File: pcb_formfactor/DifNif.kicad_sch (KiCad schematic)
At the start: 27 parts, among them J2 PROG, J4 HPLA_PORT, U1 ICE40HX4K-TQ144, U13 Teensy4_1, U2 SST26VF080A-104I/SN, X1 ASE-xxxMHz

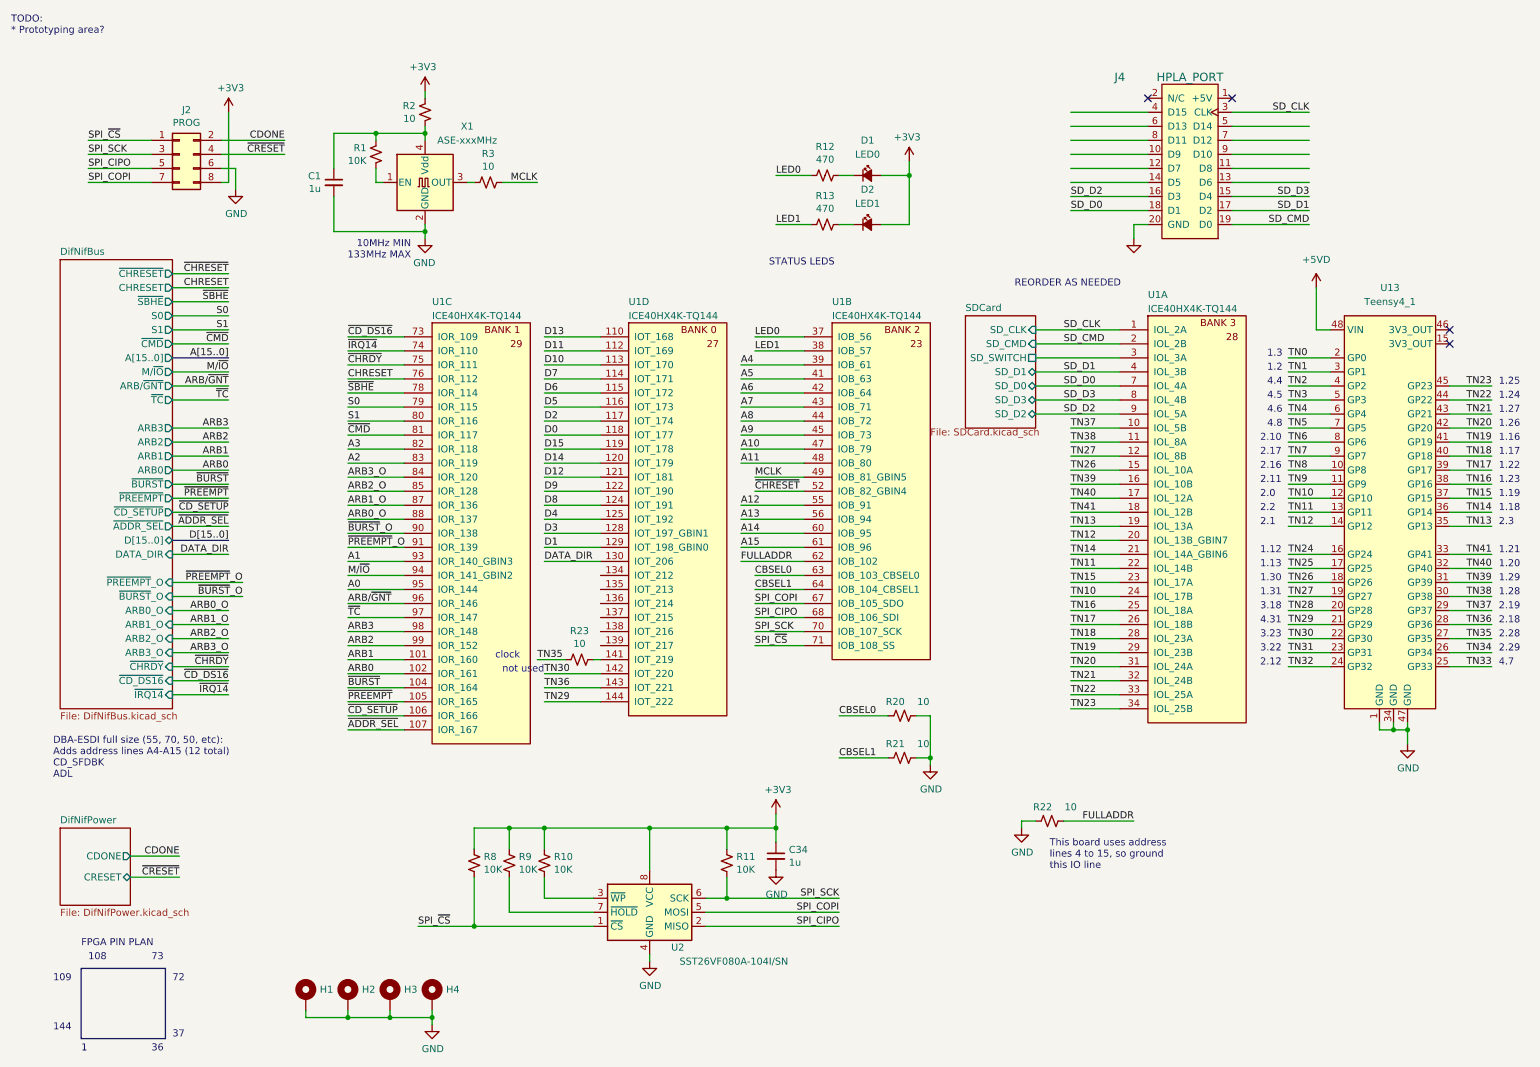
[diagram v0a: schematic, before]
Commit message: Rev P2 schematic: CHRESET fix, 74LVC8T245, -CD SFDBK, debug header
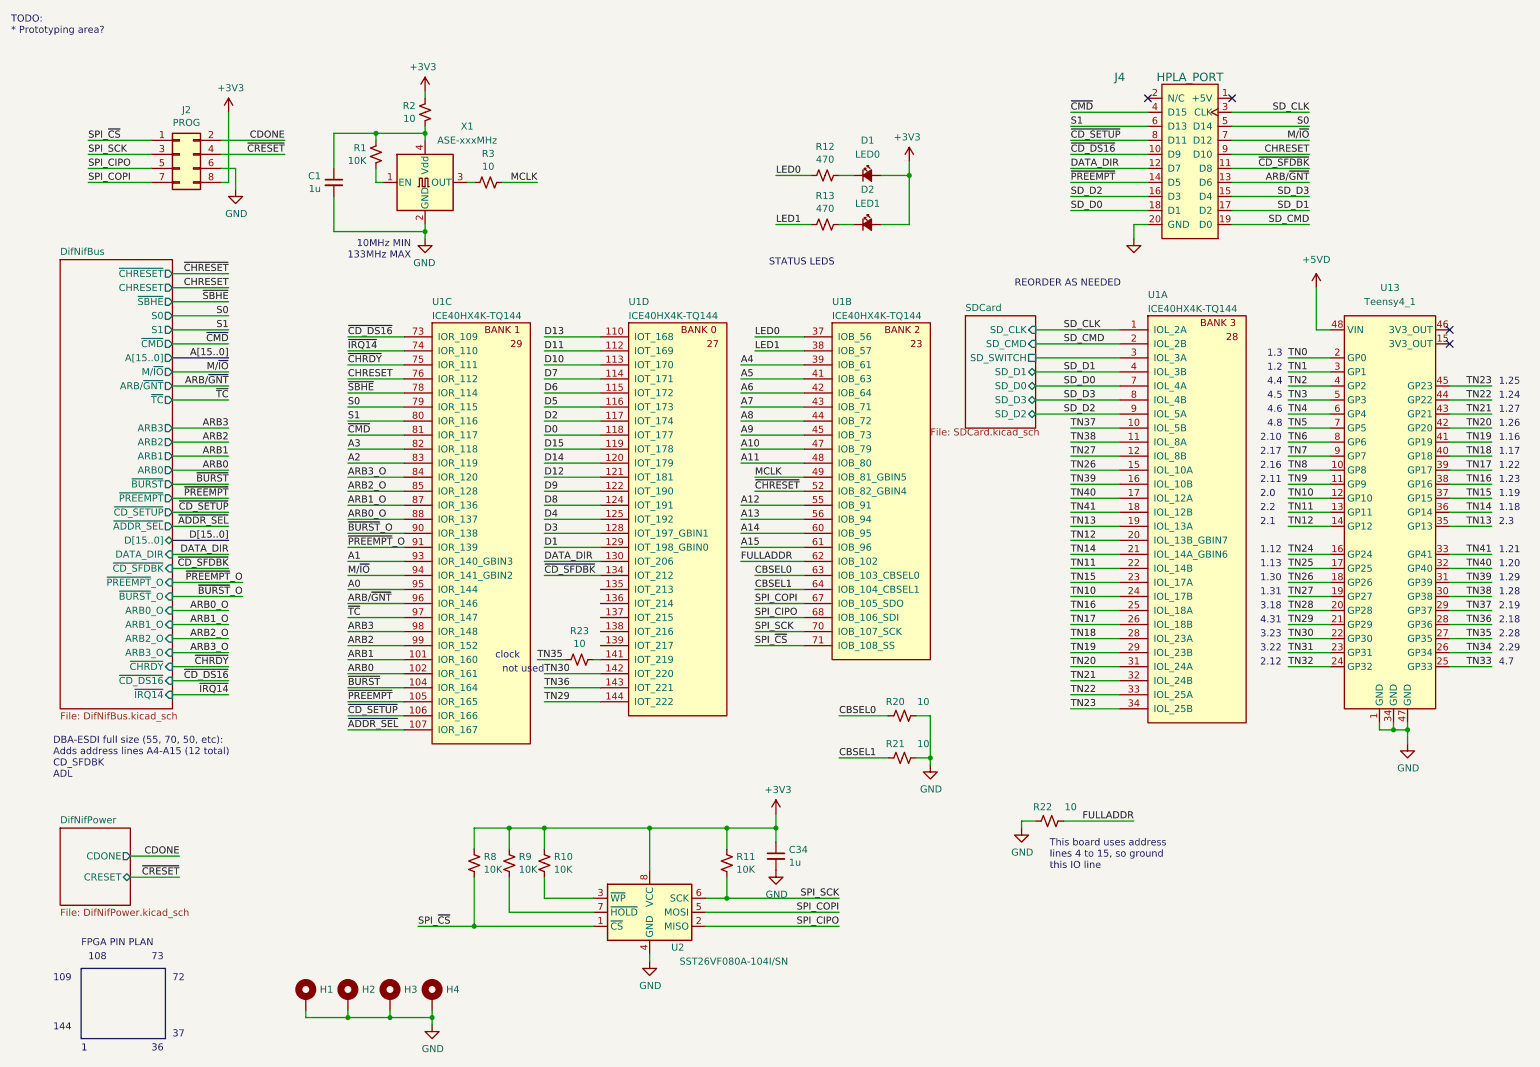
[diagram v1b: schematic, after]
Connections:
- net ARB/~{GNT}: now also J4.13 (D6)
- net CHRESET: now also J4.9 (D10)
- net DATA_DIR: now also J4.12 (D7)
- net M/~{IO}: now also J4.7 (D12)
- net S0: now also J4.5 (D14)
- net S1: now also J4.6 (D13)
- net ~{CD_DS16}: now also J4.10 (D9)
- net ~{CD_SETUP}: now also J4.8 (D11)
- net ~{CMD}: now also J4.4 (D15)
- net ~{PREEMPT}: now also J4.14 (D5)
- net ~{CD_SFDBK}: now reaches U1.134 (IOT_212)
- net ~{CD_SFDBK}: now also J4.11 (D8)
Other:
- sheet DifNifBus ports: added ~{CD_SFDBK}; removed none
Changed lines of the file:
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@@
     (effects (font (size 1.27 1.27)) (justify right bottom))
+  )
+  (wire (pts (xy 39.37 105.41) (xy 49.53 105.41))
+    (stroke (width 0) (type default) (color 0 0 0 0))
+  )
+  (label "~{CD_SFDBK}" (at 49.53 105.41 180)
+    (effects (font (size 1.27 1.27)) (justify right bottom))
+  )
+  (wire (pts (xy 106.68 106.68) (xy 116.84 106.68))
+    (stroke (width 0) (type default) (color 0 0 0 0))
+  )
+  (label "~{CD_SFDBK}" (at 106.68 106.68 0)
+    (effects (font (size 1.27 1.27)) (justify left bottom))
+  )
+  (label "~{CMD}" (at 201.93 22.86 0)
+    (effects (font (size 1.27 1.27)) (justify left bottom))
+  )
+  (label "S0" (at 245.11 25.4 180)
+    (effects (font (size 1.27 1.27)) (justify right bottom))
+  )
+  (label "S1" (at 201.93 25.4 0)
+    (effects (font (size 1.27 1.27)) (justify left bottom))
+  )
+  (label "M{slash}~{IO}" (at 245.11 27.94 180)
+    (effects (font (size 1.27 1.27)) (justify right bottom))
+  )
+  (label "~{CD_SETUP}" (at 201.93 27.94 0)
+    (effects (font (size 1.27 1.27)) (justify left bottom))
+  )
+  (label "CHRESET" (at 245.11 30.48 180)
+    (effects (font (size 1.27 1.27)) (justify right bottom))
+  )
+  (label "~{CD_DS16}" (at 201.93 30.48 0)
+    (effects (font (size 1.27 1.27)) (justify left bottom))
+  )
+  (label "~{CD_SFDBK}" (at 245.11 33.02 180)
+    (effects (font (size 1.27 1.27)) (justify right bottom))
+  )
+  (label "DATA_DIR" (at 201.93 33.02 0)
+    (effects (font (size 1.27 1.27)) (justify left bottom))
+  )
+  (label "ARB{slash}~{GNT}" (at 245.11 35.56 180)
+    (effects (font (size 1.27 1.27)) (justify right bottom))
+  )
+  (label "~{PREEMPT}" (at 201.93 35.56 0)
+    (effects (font (size 1.27 1.27)) (justify left bottom))
   )
   (label "SD_CLK" (at 245.11 22.86 180)
@@
       (effects (font (size 1.27 1.27)) (justify right))
     )
+    (pin "~{CD_SFDBK}" input (at 39.37 105.41 0)
+      (effects (font (size 1.27 1.27)) (justify right))
+    )
     (pin "~{CD_DS16}" input (at 39.37 125.73 0)
       (effects (font (size 1.27 1.27)) (justify right))
@@
       (reference "#PWR04") (unit 1) (value "GND") (footprint "")
     )
-    (path "/78d98f44-3152-4de7-839f-c3effe832ce2/c26e1f2c-806a-4b2f-a749-60d466f3e670"
-      (reference "#PWR05") (unit 1) (value "GND") (footprint "")
-    )
     (path "/78d98f44-3152-4de7-839f-c3effe832ce2/e9cf55a5-c869-4634-b9c2-d466b80e4c2e"
       (reference "#PWR06") (unit 1) (value "GND") (footprint "")
@@
     )
     (path "/78d98f44-3152-4de7-839f-c3effe832ce2/6a0d192a-3303-48e8-b5be-3e1ea48160c4"
-      (reference "U6") (unit 1) (value "74LVC4245") (footprint "Active:TSOP65P640X120-24")
+      (reference "U6") (unit 1) (value "74LVC8T245") (footprint "Active:TSOP65P640X120-24")
     )
     (path "/78d98f44-3152-4de7-839f-c3effe832ce2/60a42fa2-9611-47fe-8d44-493ed1a992b4"
-      (reference "U7") (unit 1) (value "74LVC4245") (footprint "Active:TSOP65P640X120-24")
+      (reference "U7") (unit 1) (value "74LVC8T245") (footprint "Active:TSOP65P640X120-24")
     )
     (path "/78d98f44-3152-4de7-839f-c3effe832ce2/ef0cbbd3-9218-4ba7-81cf-9535b755052c"
-      (reference "U8") (unit 1) (value "74LVC4245") (footprint "Active:TSOP65P640X120-24")
+      (reference "U8") (unit 1) (value "74LVC8T245") (footprint "Active:TSOP65P640X120-24")
     )
     (path "/78d98f44-3152-4de7-839f-c3effe832ce2/31d9ff12-65d5-46c5-b37d-36c2a19fb857"
-      (reference "U9") (unit 1) (value "74LVC4245") (footprint "Active:TSOP65P640X120-24")
+      (reference "U9") (unit 1) (value "74LVC8T245") (footprint "Active:TSOP65P640X120-24")
     )
     (path "/78d98f44-3152-4de7-839f-c3effe832ce2/f1277e00-6824-4a80-b244-d6e8b685b67f"
-      (reference "U10") (unit 1) (value "74LVC4245") (footprint "Active:TSOP65P640X120-24")
+      (reference "U10") (unit 1) (value "74LVC8T245") (footprint "Active:TSOP65P640X120-24")
     )
     (path "/78d98f44-3152-4de7-839f-c3effe832ce2/9a9b6ae8-8ab2-4caa-b7a8-ddbc8e9c1081"
@@
     )
     (path "/78d98f44-3152-4de7-839f-c3effe832ce2/328b0cf1-0e00-4564-8bd7-1543f7772a43"
-      (reference "U14") (unit 1) (value "74LVC4245") (footprint "Active:TSOP65P640X120-24")
+      (reference "U14") (unit 1) (value "74LVC8T245") (footprint "Active:TSOP65P640X120-24")
     )
     (path "/58c0945f-31b0-4f25-b315-dccac0ec690d"
